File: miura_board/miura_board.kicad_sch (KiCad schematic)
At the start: 52 parts, among them J1 Conn_01x02_Male, J2 Conn_01x02_Male, J3 Conn_01x02_Male, J4 Conn_01x04_Male, J5 Conn_01x02_Male, J6 Conn_01x02_Male, J7 Conn_01x02_Male, J8 Conn_01x02_Male, SW1 SW_Push, SW2 SW_Push, U1 ESP32-WROOM, U2 AMS1117, U3 DRV8833PW, U4 DRV8833PW, U5 AMS1117, U6 MPU-6050, U7 W25Q128JVS, U8 DRV8833PW

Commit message: Rehaul
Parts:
- removed C18, C20, C22: 2.2uF, Capacitor_SMD:C_0603_1608Metric, symbol Device:C_Small
- removed C19, C21, C27, C28: 0.1uF, Capacitor_SMD:C_0603_1608Metric, symbol Device:C_Small
- removed C23, C24, C25: 10uF, Capacitor_SMD:C_0603_1608Metric, symbol Device:C_Small
- removed J1, J2, J3, J5, J7, J8: Conn_01x02_Male, Connector_PinHeader_1.00mm:PinHeader_1x02_P1.00mm_Vertical, symbol Connector:Conn_01x02_Male
- removed U3, U4, U8: DRV8833PW, Package_SO:TSSOP-16_4.4x5mm_P0.65mm, symbol Driver_Motor:DRV8833PW
- removed U7: W25Q128JVS, Package_SO:SOIC-8_5.23x5.23mm_P1.27mm, symbol Memory_Flash:W25Q128JVS
- added J1: Micro_SD_Card_Det, Connector_Card:microSD_HC_Molex_104031-0811, symbol Connector:Micro_SD_Card_Det
- added J2: Conn_01x04_Male, Connector_PinHeader_2.54mm:PinHeader_1x04_P2.54mm_Vertical, symbol Connector:Conn_01x04_Male
- added R2: 4.7K, Resistor_SMD:R_0603_1608Metric, symbol Device:R_Small
- added R3, R4: 5.1k, Resistor_SMD:R_0603_1608Metric_Pad0.98x0.95mm_HandSolder, symbol Device:R_Small
- added U3: CP2102N-Axx-xQFN28, Package_DFN_QFN:QFN-28-1EP_5x5mm_P0.5mm_EP3.35x3.35mm, symbol Interface_USB:CP2102N-Axx-xQFN28
- added U4: MCP73832-5-OT, Package_TO_SOT_SMD:SOT-23-5, symbol Battery_Management:MCP73832-5-OT
- added USB1: HRO-TYPE-C-31-M-12, Type-C:HRO-TYPE-C-31-M-12, symbol Type-C:HRO-TYPE-C-31-M-12
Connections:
- net +3V3: now also C17.2, J1.4 (VDD), J2.4 (Pin_4), R2.1, U3.6 (VDD)
- net CS: now also J1.2 (DAT3/CD)
- net GND: now also C17.1, J1.11 (SHIELD), J1.6 (VSS), J2.3 (Pin_3), R3.2, R4.2, U3.29 (GND), U3.3 (GND), USB1.1 (GND), USB1.12 (GND), USB1.13 (SHIELD)
- net MISO: now also J1.7 (DAT0)
- net MOSI: now also J1.3 (CMD)
- net MOTOR_SUPPLY: no longer C17.1
- net RXD0: now also J2.2 (Pin_2), U3.25 (RXD)
- net SCLK: now also J1.5 (CLK)
- net TXD0: now also J2.1 (Pin_1), U3.26 (TXD)
- net VBAT: now also U4.3 (VBAT)
- new net: R3.1, USB1.4 (CC1)
- new net: R4.1, USB1.10 (CC2)
- new net: U3.4 (D+), USB1.6 (DP1)
- new net: U3.5 (D-), USB1.7 (DN1)
- new net: J1.10 (DET_A), R2.2
- new net VBUS: U3.7 (VREGIN), U3.8 (VBUS), USB1.11 (VBUS), USB1.2 (VBUS)
- no-connect marks 17 -> 24
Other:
- note added: "Logic Low - No Card Logic High - Yes Card"
- note removed: "External memory"

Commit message: Routing done
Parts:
- added C18, C19, C20: 10uF, Capacitor_SMD:C_0603_1608Metric, symbol Device:C_Small
- added D1: LED, Diode_SMD:D_0603_1608Metric, symbol Device:LED
- added R5, R6: 4.7K, Resistor_SMD:R_0603_1608Metric, symbol Device:R_Small
- J2, J4: footprint Connector_PinHeader_2.54mm:PinHeader_1x04_P2.54mm_Vertical -> Connector_PinHeader_1.27mm:PinHeader_1x04_P1.27mm_Vertical
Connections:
- net +3V3: now also C19.1, C20.1; no longer J2.4 (Pin_4), J4.4 (Pin_4)
- net GND: now also U4.2 (VSS), C18.2, C19.2, C20.2, R5.2
- net MOTOR_SUPPLY: now also J2.4 (Pin_4), J4.4 (Pin_4)
- net VBUS: now also U4.4 (VDD), C18.1, D1.2 (A)
- net at U4.1 (STAT): now also R6.1
- net at U4.5 (PROG): now also R5.1
- new net: D1.1 (K), R6.2
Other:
- note added: "~212mA constant current LED turns off when charging is complete"
- moved on the sheet: J4, U4

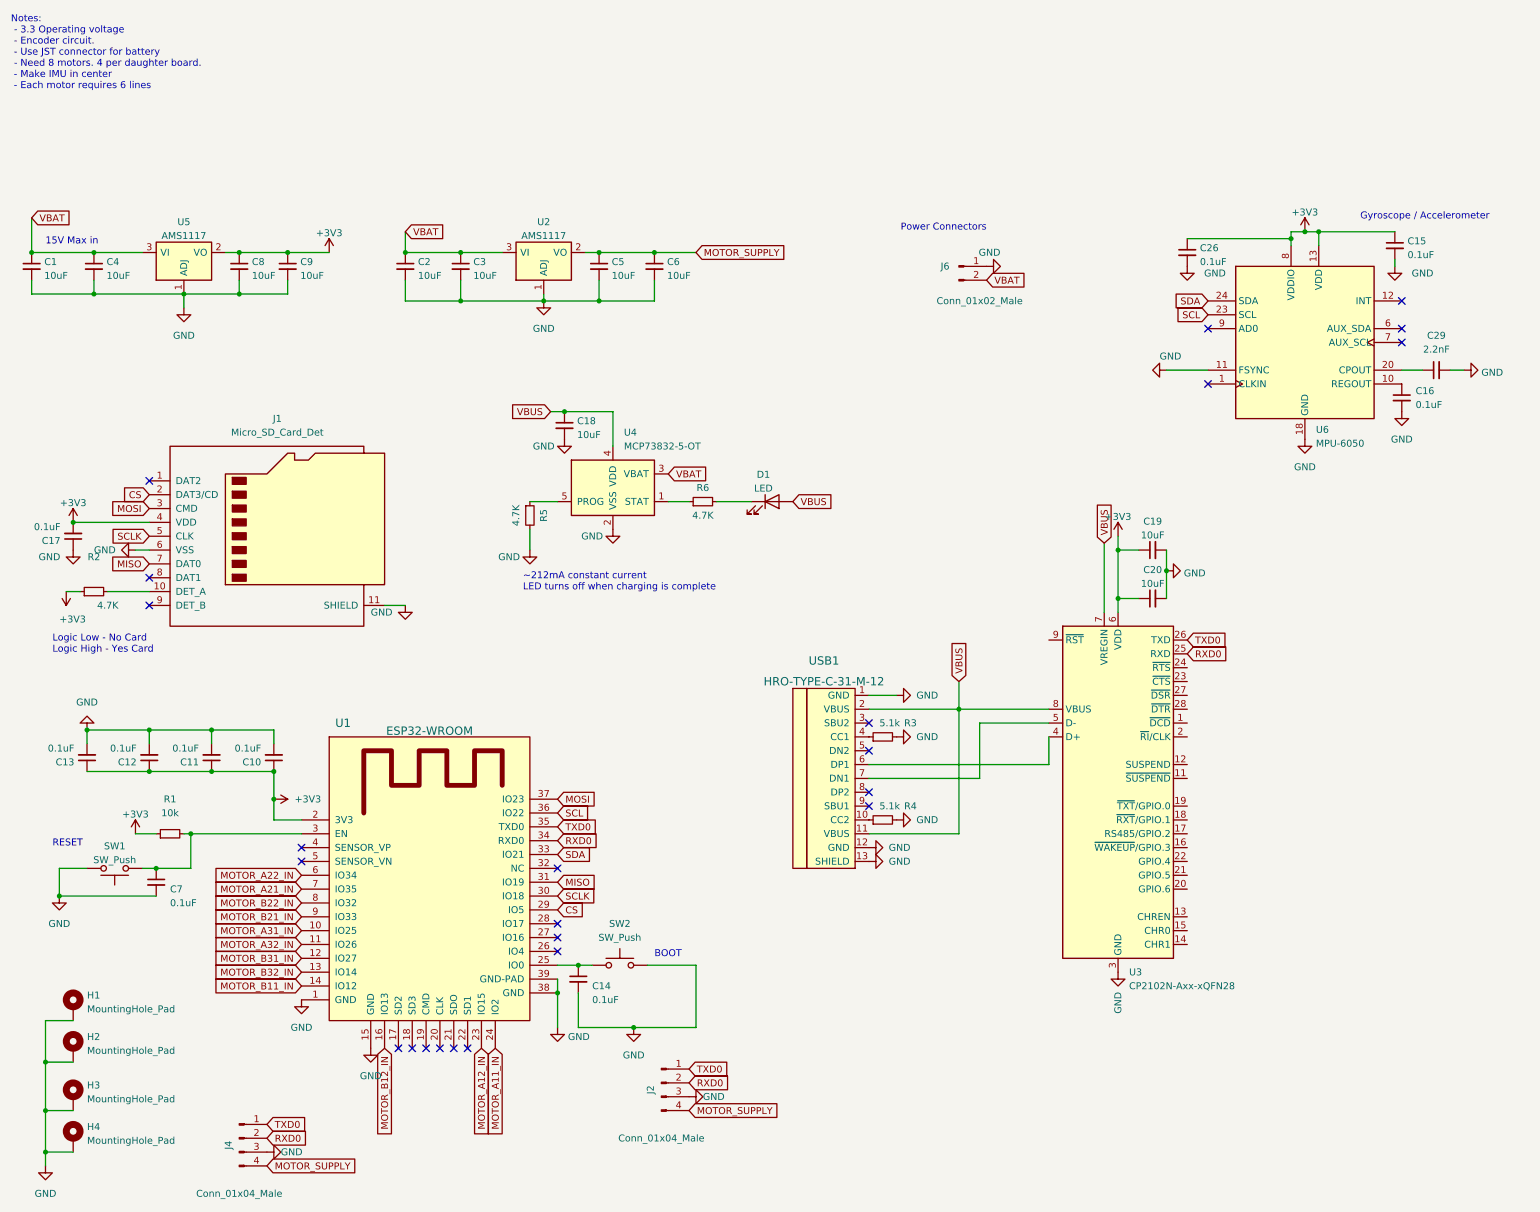
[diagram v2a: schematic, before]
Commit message: Added switch
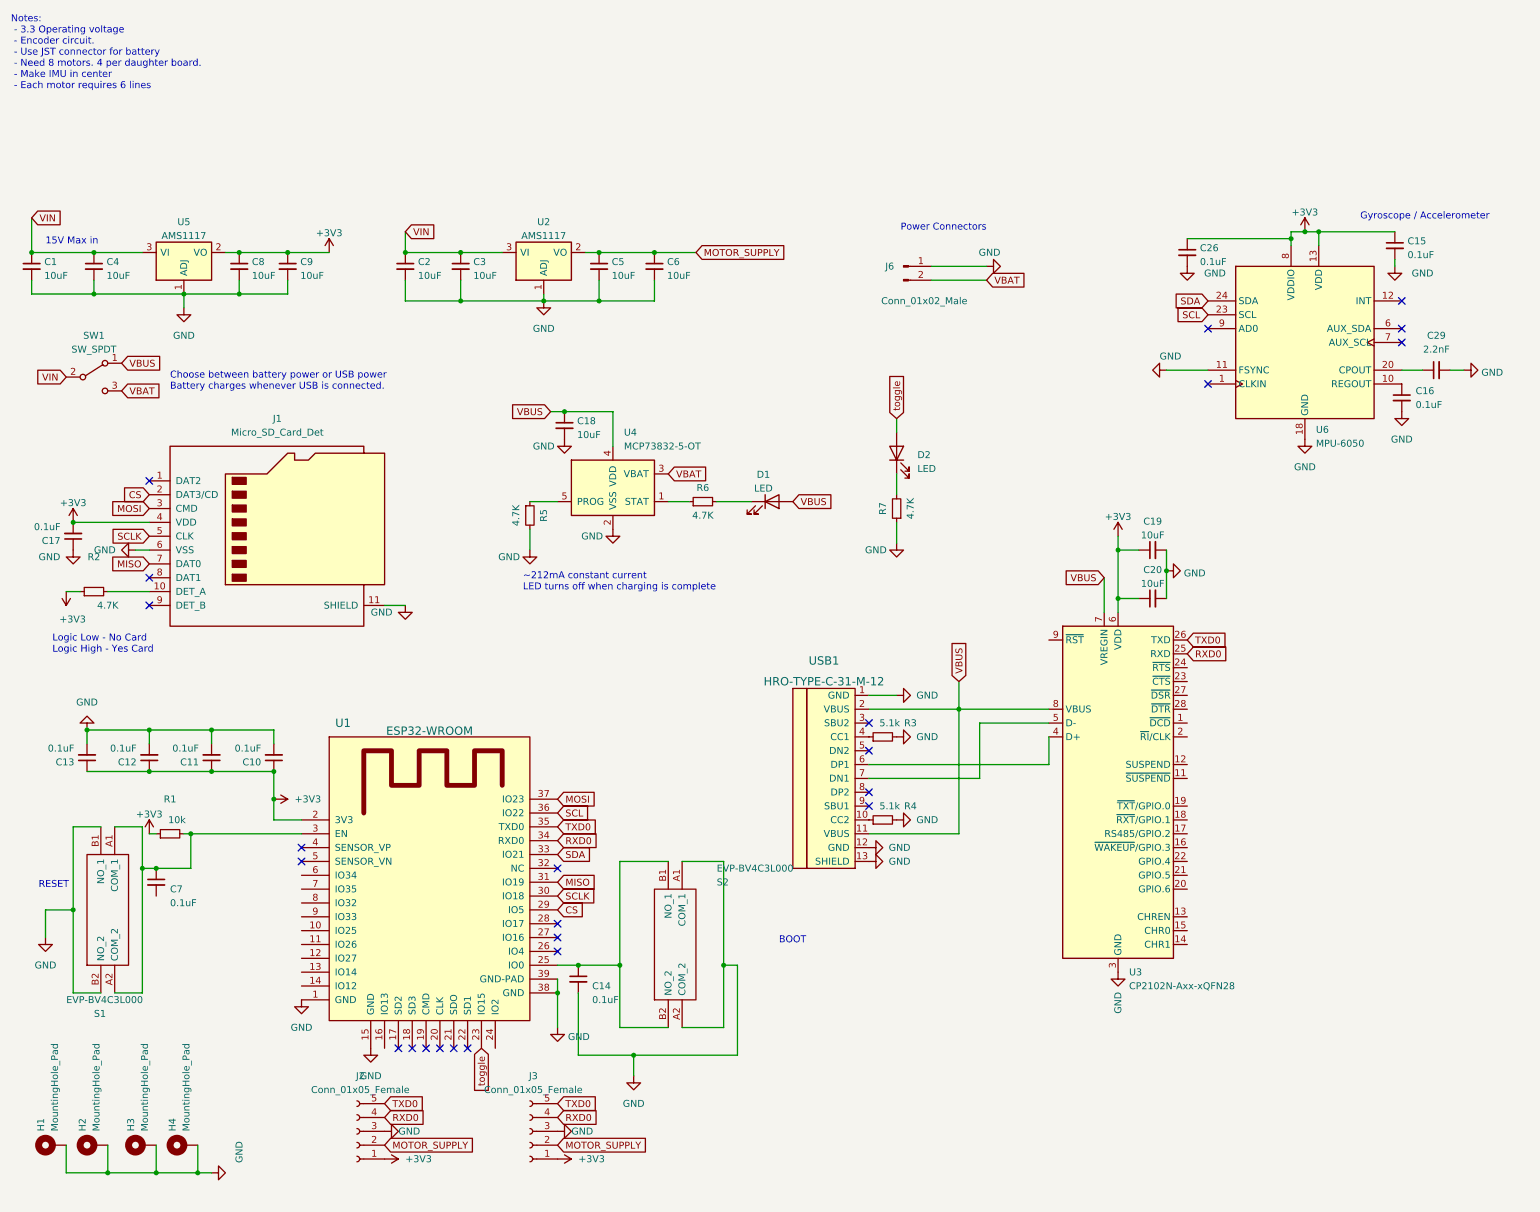
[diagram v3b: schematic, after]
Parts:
- removed J2, J4: Conn_01x04_Male, Connector_PinHeader_1.27mm:PinHeader_1x04_P1.27mm_Vertical, symbol Connector:Conn_01x04_Male
- removed SW1, SW2: SW_Push, Button_Switch_SMD:SW_SPST_EVPBF, symbol Switch:SW_Push
- added D2: LED, Diode_SMD:D_0603_1608Metric, symbol Device:LED
- added J2, J3: Conn_01x05_Female, symbol Connector:Conn_01x05_Female
- added R7: 4.7K, Resistor_SMD:R_0603_1608Metric, symbol Device:R_Small
- added S1, S2: EVP-BV4C3L000, EVPBVC_TactileSw:EVPBV4C3L000, symbol EVP-BV4C3L000:EVP-BV4C3L000
- added SW1: SW_SPDT, Button_Switch_SMD:SW_SPDT_CK-JS102011SAQN, symbol Switch:SW_SPDT
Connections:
- net +3V3: now also J2.1 (Pin_1), J3.1 (Pin_1)
- net GND: now also J2.3 (Pin_3), J3.3 (Pin_3), R7.1, S1.B1 (NO_1), S1.B2 (NO_2), S2.A1 (COM_1), S2.A2 (COM_2); no longer C7.2
- net MOTOR_SUPPLY: now also J2.2 (Pin_2), J3.2 (Pin_2)
- net RXD0: now also J2.4 (Pin_4), J3.4 (Pin_4)
- net TXD0: now also J2.5 (Pin_5), J3.5 (Pin_5)
- net VBAT: now also SW1.3 (C); no longer C1.1, C2.1, C3.1, C4.1, U2.3 (VI), U5.3 (VI)
- net VBUS: now also SW1.1 (A)
- net at C7.1, R1.2, U1.3 (EN): now also S1.A1 (COM_1), S1.A2 (COM_2)
- net at C14.1, U1.25 (IO0): now also S2.B1 (NO_1), S2.B2 (NO_2)
- net MOTOR_A11_IN: no longer names the net of U1.24 (IO2)
- net MOTOR_A12_IN renamed toggle
- net toggle: now also D2.2 (A)
- net MOTOR_A21_IN: no longer names the net of U1.7 (IO35)
- net MOTOR_A22_IN: no longer names the net of U1.6 (IO34)
- net MOTOR_A31_IN: no longer names the net of U1.10 (IO25)
- net MOTOR_A32_IN: no longer names the net of U1.11 (IO26)
- net MOTOR_B11_IN: no longer names the net of U1.14 (IO12)
- net MOTOR_B12_IN: no longer names the net of U1.16 (IO13)
- net MOTOR_B21_IN: no longer names the net of U1.9 (IO33)
- net MOTOR_B22_IN: no longer names the net of U1.8 (IO32)
- net MOTOR_B31_IN: no longer names the net of U1.12 (IO27)
- net MOTOR_B32_IN: no longer names the net of U1.13 (IO14)
- new net: D2.1 (K), R7.2
- new net VIN: C1.1, C2.1, C3.1, C4.1, SW1.2 (B), U2.3 (VI), U5.3 (VI)
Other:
- note added: "Choose between battery power or USB power Battery charges whenever USB is connected."
- moved on the sheet: H1, H2, H3, H4, J6

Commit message: Order ready
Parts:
- J1: LCSC (none) -> C585350
- J2, J3: footprint (none) -> Connector_PinHeader_1.27mm:PinHeader_1x05_P1.27mm_Vertical
- U3: LCSC (none) -> C6568
- U6: LCSC (none) -> C24112
- USB1: LCSC (none) -> C165948
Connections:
- net GND: now also J6.2 (Pin_2); no longer J6.1 (Pin_1)
- net RXD0: no longer J2.4 (Pin_4), J3.4 (Pin_4)
- net SCL: now also J2.4 (Pin_4), J3.4 (Pin_4)
- net SDA: now also J2.5 (Pin_5), J3.5 (Pin_5)
- net TXD0: no longer J2.5 (Pin_5), J3.5 (Pin_5)
- net VBAT: now also J6.1 (Pin_1); no longer J6.2 (Pin_2)
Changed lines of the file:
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@@
+    (stroke (width 0) (type default) (color 0 0 0 0))
+  )
+  (wire (pts (xy 179.07 24.13) (xy 181.61 24.13))
     (stroke (width 0) (type default) (color 0 0 0 0))
   )
@@
     (stroke (width 0) (type default) (color 0 0 0 0))
   )
+  (wire (pts (xy 179.07 26.67) (xy 182.88 26.67))
+    (stroke (width 0) (type default) (color 0 0 0 0))
+  )
   (wire (pts (xy 114.3 152.4) (xy 110.49 152.4))
     (stroke (width 0) (type default) (color 0 0 0 0))
@@
     (stroke (width 0) (type default) (color 0 0 0 0))
   )
-  (wire (pts (xy 179.07 24.13) (xy 189.23 24.13))
-    (stroke (width 0) (type default) (color 0 0 0 0))
-  )
   (wire (pts (xy 128.27 21.59) (xy 135.89 21.59))
     (stroke (width 0) (type default) (color 0 0 0 0))
@@
   )
   (wire (pts (xy 140.97 152.4) (xy 140.97 163.83))
-    (stroke (width 0) (type default) (color 0 0 0 0))
-  )
-  (wire (pts (xy 179.07 26.67) (xy 189.23 26.67))
     (stroke (width 0) (type default) (color 0 0 0 0))
   )
@@
     )
   )
+  (global_label "SCL" (shape input) (at 110.49 180.34 0) (fields_autoplaced)
+    (effects (font (size 1.27 1.27)) (justify left))
+    (property "Intersheet References" "${INTERSHEET_REFS}" (id 0) (at 116.4107 180.2606 0)
+      (effects (font (size 1.27 1.27)) (justify left) hide)
+    )
+  )
   (global_label "VBUS" (shape input) (at 153.67 67.31 0) (fields_autoplaced)
     (effects (font (size 1.27 1.27)) (justify left))
@@
     )
   )
-  (global_label "VBAT" (shape input) (at 189.23 26.67 0) (fields_autoplaced)
-    (effects (font (size 1.27 1.27)) (justify left))
-    (property "Intersheet References" "${INTERSHEET_REFS}" (id 0) (at 196.0579 26.5906 0)
+  (global_label "VBAT" (shape input) (at 181.61 24.13 0) (fields_autoplaced)
+    (effects (font (size 1.27 1.27)) (justify left))
+    (property "Intersheet References" "${INTERSHEET_REFS}" (id 0) (at 188.4379 24.0506 0)
       (effects (font (size 1.27 1.27)) (justify left) hide)
     )
@@
     (effects (font (size 1.27 1.27)) (justify left))
     (property "Intersheet References" "${INTERSHEET_REFS}" (id 0) (at 117.6807 139.6206 0)
+      (effects (font (size 1.27 1.27)) (justify left) hide)
+    )
+  )
+  (global_label "SCL" (shape input) (at 78.74 180.34 0) (fields_autoplaced)
+    (effects (font (size 1.27 1.27)) (justify left))
+    (property "Intersheet References" "${INTERSHEET_REFS}" (id 0) (at 84.6607 180.2606 0)
       (effects (font (size 1.27 1.27)) (justify left) hide)
     )
@@
     )
   )
-  (global_label "RXD0" (shape input) (at 110.49 180.34 0) (fields_autoplaced)
-    (effects (font (size 1.27 1.27)) (justify left))
-    (property "Intersheet References" "${INTERSHEET_REFS}" (id 0) (at 117.8621 180.2606 0)
-      (effects (font (size 1.27 1.27)) (justify left) hide)
-    )
-  )
   (global_label "CS" (shape input) (at 35.56 66.04 180) (fields_autoplaced)
     (effects (font (size 1.27 1.27)) (justify right))
@@
     )
   )
+  (global_label "SDA" (shape input) (at 78.74 177.8 0) (fields_autoplaced)
+    (effects (font (size 1.27 1.27)) (justify left))
+    (property "Intersheet References" "${INTERSHEET_REFS}" (id 0) (at 84.7212 177.7206 0)
+      (effects (font (size 1.27 1.27)) (justify left) hide)
+    )
+  )
+  (global_label "SDA" (shape input) (at 110.49 177.8 0) (fields_autoplaced)
+    (effects (font (size 1.27 1.27)) (justify left))
+    (property "Intersheet References" "${INTERSHEET_REFS}" (id 0) (at 116.4712 177.7206 0)
+      (effects (font (size 1.27 1.27)) (justify left) hide)
+    )
+  )
   (global_label "MOSI" (shape input) (at 110.49 121.92 0) (fields_autoplaced)
     (effects (font (size 1.27 1.27)) (justify left))
@@
     )
   )
-  (global_label "RXD0" (shape input) (at 78.74 180.34 0) (fields_autoplaced)
-    (effects (font (size 1.27 1.27)) (justify left))
-    (property "Intersheet References" "${INTERSHEET_REFS}" (id 0) (at 86.1121 180.2606 0)
-      (effects (font (size 1.27 1.27)) (justify left) hide)
-    )
-  )
   (global_label "MOTOR_SUPPLY" (shape input) (at 78.74 185.42 0) (fields_autoplaced)
     (effects (font (size 1.27 1.27)) (justify left))
@@
     )
   )
-  (global_label "TXD0" (shape input) (at 110.49 177.8 0) (fields_autoplaced)
-    (effects (font (size 1.27 1.27)) (justify left))
-    (property "Intersheet References" "${INTERSHEET_REFS}" (id 0) (at 117.5598 177.7206 0)
-      (effects (font (size 1.27 1.27)) (justify left) hide)
-    )
-  )
   (global_label "TXD0" (shape input) (at 226.06 92.71 0) (fields_autoplaced)
     (effects (font (size 1.27 1.27)) (justify left))
     (property "Intersheet References" "${INTERSHEET_REFS}" (id 0) (at 233.1298 92.6306 0)
-      (effects (font (size 1.27 1.27)) (justify left) hide)
-    )
-  )
-  (global_label "TXD0" (shape input) (at 78.74 177.8 0) (fields_autoplaced)
-    (effects (font (size 1.27 1.27)) (justify left))
-    (property "Intersheet References" "${INTERSHEET_REFS}" (id 0) (at 85.8098 177.7206 0)
       (effects (font (size 1.27 1.27)) (justify left) hide)
     )
@@
     )
     (property "Datasheet" "https://store.invensense.com/datasheets/invensense/MPU-6050_DataSheet_V3%204.pdf" (id 3) (at 247.65 41.91 0)
+      (effects (font (size 1.27 1.27)) hide)
+    )
+    (property "LCSC" "C24112" (id 4) (at 247.65 38.1 0)
       (effects (font (size 1.27 1.27)) hide)
     )
@@
     (pin "2")
   )
-  (symbol (lib_id "power:GND") (at 189.23 24.13 90) (unit 1)
-    (in_bom yes) (on_board yes)
-    (property "Reference" "#PWR0120" (id 0) (at 195.58 24.13 0)
-      (effects (font (size 1.27 1.27)) hide)
-    )
-    (property "Value" "GND" (id 1) (at 191.77 21.59 90)
-      (effects (font (size 1.27 1.27)) (justify left))
-    )
-    (property "Footprint" "" (id 2) (at 189.23 24.13 0)
-      (effects (font (size 1.27 1.27)) hide)
-    )
-    (property "Datasheet" "" (id 3) (at 189.23 24.13 0)
+  (symbol (lib_id "power:GND") (at 182.88 26.67 90) (unit 1)
+    (in_bom yes) (on_board yes)
+    (property "Reference" "#PWR0120" (id 0) (at 189.23 26.67 0)
+      (effects (font (size 1.27 1.27)) hide)
+    )
+    (property "Value" "GND" (id 1) (at 190.5 26.67 90)
+      (effects (font (size 1.27 1.27)) (justify left))
+    )
+    (property "Footprint" "" (id 2) (at 182.88 26.67 0)
+      (effects (font (size 1.27 1.27)) hide)
+    )
+    (property "Datasheet" "" (id 3) (at 182.88 26.67 0)
       (effects (font (size 1.27 1.27)) hide)
     )
@@
   )
   (symbol (lib_id "power:GND") (at 76.2 167.64 0) (unit 1)
-    (in_bom yes) (on_board yes) (fields_autoplaced)
+    (in_bom yes) (on_board yes)
     (property "Reference" "#PWR0114" (id 0) (at 76.2 173.99 0)
       (effects (font (size 1.27 1.27)) hide)
     )
-    (property "Value" "GND" (id 1) (at 76.2 172.72 0))
+    (property "Value" "GND" (id 1) (at 78.74 171.45 0))
     (property "Footprint" "" (id 2) (at 76.2 167.64 0)
       (effects (font (size 1.27 1.27)) hide)
@@
     (property "Datasheet" "" (id 3) (at 165.1 116.84 0)
       (effects (font (size 1.524 1.524)) hide)
+    )
+    (property "LCSC" "C165948" (id 4) (at 165.1 116.84 0)
+      (effects (font (size 1.27 1.27)) hide)
     )
     (pin "1")
@@
     )
     (property "Datasheet" "https://www.silabs.com/documents/public/data-sheets/cp2102n-datasheet.pdf" (id 3) (at 214.63 139.7 0)
+      (effects (font (size 1.27 1.27)) hide)
+    )
+    (property "LCSC" "C6568" (id 4) (at 213.36 120.65 0)
       (effects (font (size 1.27 1.27)) hide)
     )
@@
     (property "Reference" "J2" (id 0) (at 74.295 172.72 0))
     (property "Value" "Conn_01x05_Female" (id 1) (at 74.295 175.26 0))
-    (property "Footprint" "" (id 2) (at 73.66 182.88 0)
+    (property "Footprint" "Connector_PinHeader_1.27mm:PinHeader_1x05_P1.27mm_Vertical" (id 2) (at 73.66 182.88 0)
       (effects (font (size 1.27 1.27)) hide)
     )
@@
     )
     (property "Datasheet" "https://www.hirose.com/product/en/download_file/key_name/DM3/category/Catalog/doc_file_id/49662/?file_category_id=4&item_id=195&is_series=1" (id 3) (at 58.42 71.12 0)
+      (effects (font (size 1.27 1.27)) hide)
+    )
+    (property "LCSC" "C585350" (id 4) (at 58.42 73.66 0)
       (effects (font (size 1.27 1.27)) hide)
     )
@@
     (property "Reference" "J3" (id 0) (at 106.045 172.72 0))
     (property "Value" "Conn_01x05_Female" (id 1) (at 106.045 175.26 0))
-    (property "Footprint" "" (id 2) (at 105.41 182.88 0)
+    (property "Footprint" "Connector_PinHeader_1.27mm:PinHeader_1x05_P1.27mm_Vertical" (id 2) (at 105.41 182.88 0)
       (effects (font (size 1.27 1.27)) hide)
     )
@@
       (effects (font (size 1.27 1.27)) (justify right))
     )
-    (property "Value" "EVP-BV4C3L000" (id 1) (at 139.7 134.62 90)
+    (property "Value" "EVP-BV4C3L000" (id 1) (at 137.16 142.24 90)
       (effects (font (size 1.27 1.27)) (justify right))
     )
@@
     )
     (path "/8220bfd3-e338-4eb1-8379-1f5d265d7a1d"
-      (reference "J2") (unit 1) (value "Conn_01x05_Female") (footprint "")
+      (reference "J2") (unit 1) (value "Conn_01x05_Female") (footprint "Connector_PinHeader_1.27mm:PinHeader_1x05_P1.27mm_Vertical")
     )
     (path "/b732d140-d52a-40a3-90f0-07fbed1e598e"
-      (reference "J3") (unit 1) (value "Conn_01x05_Female") (footprint "")
+      (reference "J3") (unit 1) (value "Conn_01x05_Female") (footprint "Connector_PinHeader_1.27mm:PinHeader_1x05_P1.27mm_Vertical")
     )
     (path "/87d11127-0c82-4d4b-9ddd-58e6fdb20771"
